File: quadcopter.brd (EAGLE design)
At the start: 196 x 196 mm, 65 parts, among them J1 ISP, U1 ATMEGA128RFA1

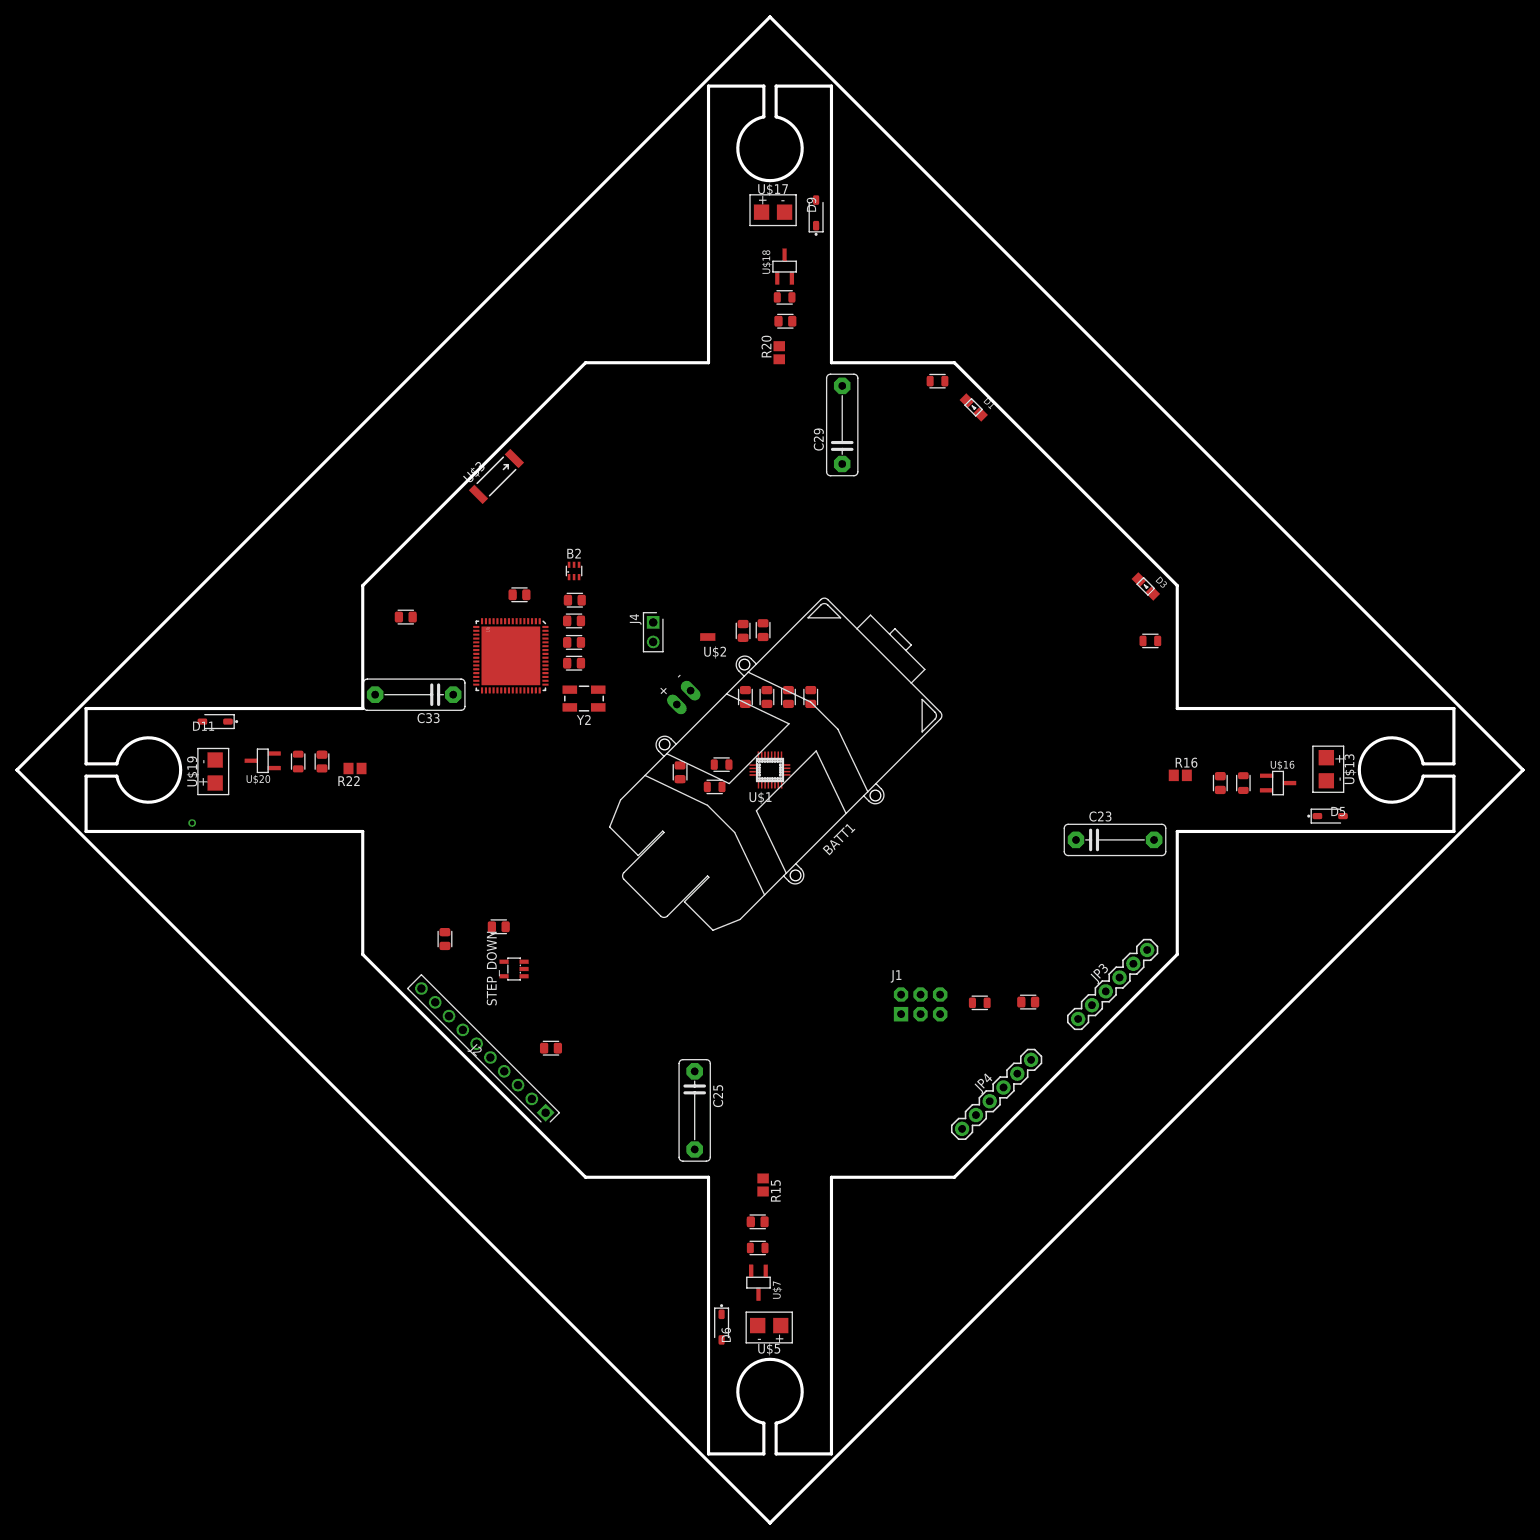
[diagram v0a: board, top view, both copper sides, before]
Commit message: There surely are a ton of mistakes, but I'm not sure what they are. I had to do a ton of routing by hand
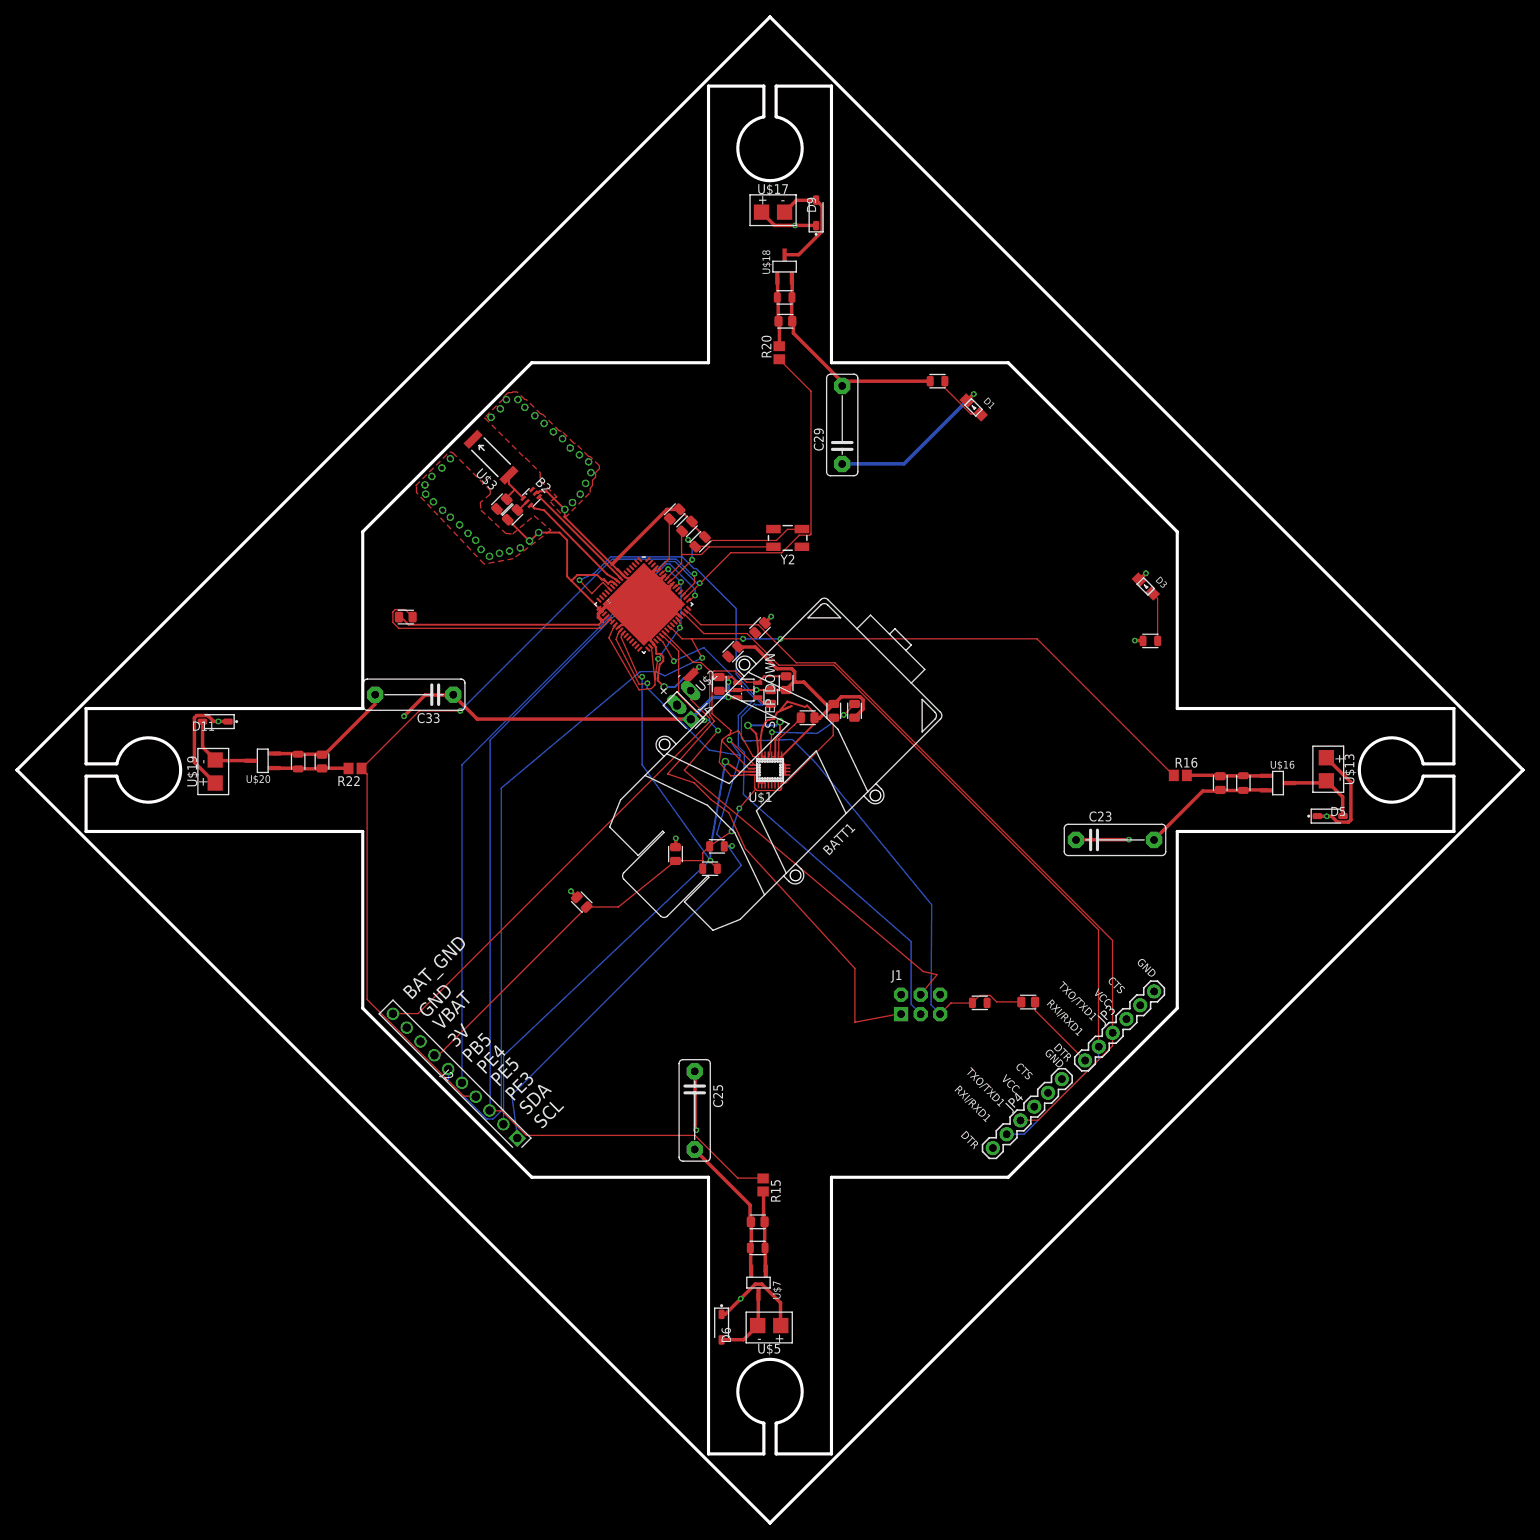
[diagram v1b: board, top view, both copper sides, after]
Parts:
- moved C27 48.8 mm to (-6.60, 11.2)
- moved STEP_DOWN 47.3 mm to (-2.90, 10.4), turned to 270 degrees
- moved C13 46.3 mm to (0.10, 9.50), turned to 90 degrees
- moved Y2 33.7 mm to (2.30, 30.2)
- moved C1 22.8 mm to (-9.10, 29.7), turned to 45 degrees
- moved C2 21.1 mm to (-10.8, 31.7), turned to 45 degrees
- moved C28 19.4 mm to (-24.5, -17.2), turned to 135 degrees
- moved C6 19.1 mm to (-12.4, 33.3), turned to 45 degrees
- moved U1 18.6 mm to (-16.4, 21.6), turned to 315 degrees
- moved C7 13.7 mm to (-33.5, 33.2), turned to 45 degrees
- moved J4 13.5 mm to (-10.3, 6.60), turned to 135 degrees
- moved C8 12.0 mm to (-34.9, 34.6), turned to 225 degrees
- moved B2 11.1 mm to (-31.1, 35.5), turned to 315 degrees
- moved R7 10.7 mm to (-7.80, -12.8)
- moved C11 10.7 mm to (-12.3, -10.9)
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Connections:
- net N$1 renamed JUMPER_INPUT
- net N$9 renamed DTR
- removed net N$21: C27.1, STEP_DOWN.1
- removed net N$22: STEP_DOWN.2
- removed net N$27: STEP_DOWN.3
- removed net N$8: JP3.GND, JP4.GND
- net BAT_GND: no longer C27.2
- net GND: now also C27.2, JP3.GND, JP4.GND, STEP_DOWN.2
- net PB5: now also J2.6
- net PE3: now also J2.3
- net PE4: now also J2.5
- net PE5: now also J2.4
- net SCL: now also J2.1
- net SDA: now also J2.2
- net VBAT: now also C27.1, STEP_DOWN.1, STEP_DOWN.3
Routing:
- net GND: track 0.00 -> 293.9 mm, vias 1 -> 42
- net PB5: track 0.00 -> 161.7 mm, vias 0 -> 3
- net VBAT: track 0.00 -> 142.8 mm, vias 0 -> 11
- net 3V: track 0.00 -> 131.6 mm, vias 0 -> 4
- net PE4: track 0.00 -> 128.7 mm, vias 0 -> 1
- net PE3: track 0.00 -> 126.9 mm, vias 0 -> 1
- net RESET: track 0.00 -> 111.6 mm, vias 0 -> 1
- net PE5: track 0.00 -> 108.5 mm, vias 0 -> 2
- net RXD1: track 0.00 -> 104.0 mm
- net TXD1: track 0.00 -> 103.0 mm
- net SDA: track 0.00 -> 98.2 mm, vias 0 -> 3
- net SCL: track 0.00 -> 97.7 mm, vias 0 -> 3
- net MISO: track 0.00 -> 73.0 mm
- net SCK: track 0.00 -> 70.2 mm, vias 0 -> 1
- net MOSI: track 0.00 -> 68.5 mm, vias 0 -> 2
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- added copper zone on layer 2, net 3V
- added copper zone on layer 1, net GND
- added copper zone on layer 2, net GND
- added copper zone on layer 2, net N$1
- added copper zone on layer 15, net N$14
- added copper zone on layer 2, net VBAT
- removed copper zone on layer 2, net N$11
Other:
- outline, holes or cut-outs redrawn
- board text added: "3V"
- board text added: "BAT_GND"
- board text added: "CTS"
- board text added: "DTR"
- board text added: "GND"
- board text added: "PB5"
- board text added: "PE3"
- board text added: "PE4"
- board text added: "PE5"
- board text added: "RXI/RXD1"
- board text added: "SCL"
- board text added: "SDA"
- board text added: "TXO/TXD1"
- board text added: "VBAT"
- board text added: "VCC"

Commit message: routed and everything
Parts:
- removed C23, C25, C29, C33: 100uf, capacitor-wima:C10B4
- removed R15, R16, R20, R22: 100R, Lab5:R0805
- added C14, C19, C20, C9: 220uF, quadparts_prebuilt:CAPMP7343X310_HS
- added R4, R5, R6, R9: 100, quadparts_prebuilt:RESC2012X60_HS
- moved J4 38.6 mm to (-48.6, 2.33), turned to 0 degrees
- moved C5 13.6 mm to (-36.0, 12.4)
- moved C24 4.15 mm to (54.5, -1.32)
- moved C10 2.95 mm to (-2.20, -55.9)
- moved C30 2.71 mm to (1.83, 55.7)
- moved C34 2.52 mm to (-55.9, 1.90)
- moved R17 2.51 mm to (59.1, -1.46)
- moved R23 1.60 mm to (-60.3, 2.27)
- moved U$20 1.59 mm to (-66.4, 2.75)
- moved R10 1.38 mm to (-2.30, -61.0)
- moved R21 1.34 mm to (1.93, 60.2)
- moved U$7 1.10 mm to (-2.60, -66.7)
- moved U$18 0.85 mm to (2.75, 65.5)
- moved U$16 0.27 mm to (66.2, -1.93)
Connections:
- removed net CLKI: U1.33
- removed net N$17: U$1.P$6, U$1.P$7, U$1.P$8
- removed net N$23: U1.23, U1.34, U1.44, U1.54, U1.59
- removed net N$24: R1.2
- removed net N$25: C4.1
- removed net N$26: C3.1
- removed net TST: U1.11
- net 3V: now also C3.1, C4.1, R1.2, U$1.P$6, U$1.P$7, U$1.P$8, U1.23, U1.34, U1.44, U1.54, U1.59
- net BAT_GND: now also C10.2, C14.2, C19.2, C20.2, C24.2, C27.2, C30.2, C34.2, C9.2, R10.1, R17.1, R21.1, R23.1, U$16.P$2, U$18.P$2, U$20.P$2, U$7.P$2
- net FILTERED: now also R5.2; no longer R16.2
- net FILTERED1: now also R6.2; no longer R20.2
- net FILTERED3: now also R4.2; no longer R15.2
- net FILTERED5: now also R9.2; no longer R22.2
- net GND: now also U1.11, U1.33; no longer C10.2, C23.2, C24.2, C25.2, C27.2, C29.2, C30.2, C33.2, C34.2, R10.1, R17.1, R21.1, R23.1, U$16.P$2, U$18.P$2, U$20.P$2, U$7.P$2
- net PB5: now also R5.1; no longer R16.1
- net PE3: now also R4.1; no longer R15.1
- net PE4: now also R6.1; no longer R20.1
- net PE5: now also R9.1; no longer R22.1
- net RX1: now also JP4.TXO
- net RXD1: now also JP3.TXO; no longer JP3.RXI, JP4.RXI
- net TX1: now also JP4.RXI
- net TXD1: now also JP3.RXI; no longer JP3.TXO, JP4.TXO
- net VBAT: now also C14.1, C19.1, C20.1, C9.1; no longer C23.1, C25.1, C29.1, C33.1
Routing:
- net 3V: track 131.6 -> 230.1 mm, vias 4 -> 11
- net RX1: track 0.00 -> 98.0 mm
- net TX1: track 0.00 -> 92.1 mm
- net BAT_GND: track 63.8 -> 147.5 mm, vias 0 -> 5
- net JUMPER_INPUT: track 0.14 -> 40.2 mm, vias 0 -> 1
- net N$23: track 38.5 -> 0.00 mm, vias 4 -> 0
- net PE4: track 128.7 -> 153.3 mm, vias 1 -> 2
- net RXD1: track 104.0 -> 80.5 mm, vias 0 -> 1
- net TXD1: track 103.0 -> 81.3 mm, vias 0 -> 1
- net PB5: track 161.7 -> 142.6 mm, vias 3 -> 2
- net GND: track 293.9 -> 277.7 mm, vias 42 -> 46
- net N$5: track 15.4 -> 30.8 mm, vias 2 -> 4
- net N$4: track 23.1 -> 38.0 mm, vias 2 -> 0
- net DVDD: track 34.0 -> 19.1 mm
- net FILTERED: track 10.5 -> 24.7 mm
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- added copper zone on layer 15, net BAT_GND
